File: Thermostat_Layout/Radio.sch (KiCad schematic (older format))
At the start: 15 parts, among them J4 Conn_Coaxial, U6 nRF24L01P, Y2 16MHz

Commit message: Update remote sensor layout
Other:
- moved on the sheet: C10, C11, C12, C13, C14, C8, C9, R8, R9, Y2

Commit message: Remove NRF24 from schematic
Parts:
- removed C10: 2.2nF, Capacitor_SMD:C_0402_1005Metric, symbol Device:C
- removed C11, C9: 22pF, Capacitor_SMD:C_0402_1005Metric, symbol Device:C
- removed C12: 4.7pF, Capacitor_SMD:C_0402_1005Metric, symbol Device:C
- removed C13: 15pF, Capacitor_SMD:C_0402_1005Metric, symbol Device:C
- removed C14: 1.5pF, Capacitor_SMD:C_0402_1005Metric, symbol Device:C
- removed C8: 33nF, Capacitor_SMD:C_0402_1005Metric, symbol Device:C
- removed J4: Conn_Coaxial, Connector_Coaxial:U.FL_Molex_MCRF_73412-0110_Vertical, symbol Connector:Conn_Coaxial
- removed L1: 12nH, Inductor_SMD:L_0402_1005Metric, symbol Device:L
- removed L2: 2.3nH, Inductor_SMD:L_0402_1005Metric, symbol Device:L
- removed L3: 7.9nH, Inductor_SMD:L_0402_1005Metric, symbol Device:L
- removed R8: 22kΩ, Resistors:0402, symbol Device:R_US
- removed R9: 1MΩ, Resistor_SMD:R_0402_1005Metric, symbol Device:R_US
- removed U6: nRF24L01P, Package_DFN_QFN:QFN-20-1EP_4x4mm_P0.5mm_EP2.5x2.5mm, symbol RF:nRF24L01P
- removed Y2: 16MHz, Crystal:Crystal_SMD_SeikoEpson_MC405-2Pin_9.6x4.1mm, symbol Device:Crystal
- added U?: ESP-07, RF_Module:ESP-07, symbol RF_Module:ESP-07
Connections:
- net labels removed: 3.3V, GND, MISO, MOSI, RF_CE, RF_CSN, SCK
- wire segments 42 -> 0

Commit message: Update schematic
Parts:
- gave numbers to parts that had none: 1
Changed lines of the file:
@@
 $EndDescr
 $Comp
-L RF_Module:ESP-07 U?
+L RF_Module:ESP-07 U10
 U 1 1 5D98C19F
 P 5900 3650
-F 0 "U?" H 5900 4631 50  0000 C CNN
+F 0 "U10" H 5900 4631 50  0000 C CNN
 F 1 "ESP-07" H 5900 4540 50  0000 C CNN
 F 2 "RF_Module:ESP-07" H 5900 3650 50  0001 C CNN

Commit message: Layout changes
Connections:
- net RADIO_RST: now reaches U10.1 (~RST)
- net RADIO_RX: now reaches U10.15 (GPIO3/RXD)
- net RADIO_TX: now reaches U10.16 (GPIO1/TXD)
- net RADIO_EN: now reaches U10.3 (EN)
- net 3.3V: now reaches U10.8 (VCC)
- net GND: now reaches U10.9 (GND)
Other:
- moved on the sheet: U10
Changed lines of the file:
@@
 L RF_Module:ESP-07 U10
 U 1 1 5D98C19F
-P 5900 3650
-F 0 "U10" H 5900 4631 50  0000 C CNN
-F 1 "ESP-07" H 5900 4540 50  0000 C CNN
-F 2 "RF_Module:ESP-07" H 5900 3650 50  0001 C CNN
-F 3 "http://wiki.ai-thinker.com/_media/esp8266/esp8266_series_modules_user_manual_v1.1.pdf" H 5550 3750 50  0001 C CNN
-	1    5900 3650
+P 5650 3550
+F 0 "U10" H 5650 4531 50  0000 C CNN
+F 1 "ESP-07" H 5650 4440 50  0000 C CNN
+F 2 "RF_Module:ESP-07" H 5650 3550 50  0001 C CNN
+F 3 "http://wiki.ai-thinker.com/_media/esp8266/esp8266_series_modules_user_manual_v1.1.pdf" H 5300 3650 50  0001 C CNN
+	1    5650 3550
 	1    0    0    -1
 $EndComp
+Text GLabel 6600 3050 2    50   Output ~ 0
+RADIO_TX
+Text GLabel 6600 3250 2    50   Input ~ 0
+RADIO_RX
+Wire Wire Line
+	6250 3050 6600 3050
+Wire Wire Line
+	6250 3250 6600 3250
+$Comp
+L SparkFun-PowerSymbols:3.3V #SUPPLY?
+U 1 1 5D9E7A19
+P 5650 2500
+F 0 "#SUPPLY?" H 5700 2500 45  0001 L BNN
+F 1 "3.3V" H 5650 2776 45  0000 C CNN
+F 2 "XXX-00000" H 5650 2681 60  0000 C CNN
+F 3 "" H 5650 2500 60  0001 C CNN
+	1    5650 2500
+	1    0    0    -1
+$EndComp
+$Comp
+L SparkFun-PowerSymbols:GND #GND?
+U 1 1 5D9E8201
+P 5650 4400
+F 0 "#GND?" H 5700 4350 45  0001 L BNN
+F 1 "GND" H 5650 4230 45  0000 C CNN
+F 2 "" H 5650 4300 60  0001 C CNN
+F 3 "" H 5650 4300 60  0001 C CNN
+	1    5650 4400
+	1    0    0    -1
+$EndComp
+Wire Wire Line
+	5650 4250 5650 4400
+Wire Wire Line
+	5650 2750 5650 2500
+Text GLabel 4650 2950 0    50   Input ~ 0
+RADIO_RST
+Text GLabel 4650 3150 0    50   Input ~ 0
+RADIO_EN
+Wire Wire Line
+	4650 2950 5050 2950
+Wire Wire Line
+	5050 3150 4650 3150
 $EndSCHEMATC

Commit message: Complete radio schematic
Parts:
- added J? (x2): Conn_01x03, symbol Connector_Generic:Conn_01x03
- added R? (x2): 10k, symbol Device:R_US
- added R? (x5): 1k, symbol Device:R_US
- added SW? (x2): SW_DPDT_x2, symbol Switch:SW_DPDT_x2
- added SW? (x2): SW_SPST, symbol Switch:SW_SPST
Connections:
- net 3.3V: now also R?.1, R?.1
- net GND: now also J?.2 (Pin_2), J?.2 (Pin_2), R?.2, SW?.1 (A), SW?.2 (B)
- net RADIO_EN: now also R?.2
- net RADIO_RST: now also R?.2, SW?.2 (B)
- net at U10.10 (GPIO15): now also R?.1
- net at U10.12 (GPIO0): now also SW?.1 (A)
- net DBG_RX: now reaches U10.5 (GPIO14)
- net DBG_RX: now also R?.2
- net DBG_TX: now reaches U10.6 (GPIO12)
- net DBG_TX: now also R?.2
- net RADIO_RX renamed RX
- net RX: now also SW?.5 (B)
- net RADIO_TX renamed TX
- net TX: now also SW?.2 (B)
- new net: J?.1 (Pin_1), R?.1 (x2)
- new net: J?.3 (Pin_3), R?.1 (x2)
- new net RADIO_COM_RX: SW?.4 (A)
- new net RADIO_COM_TX: SW?.1 (A)
- new net RADIO_PRG_RX: R?.2, SW?.6 (C)
- new net RADIO_PRG_TX: R?.2, SW?.3 (C)
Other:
- moved on the sheet: U10

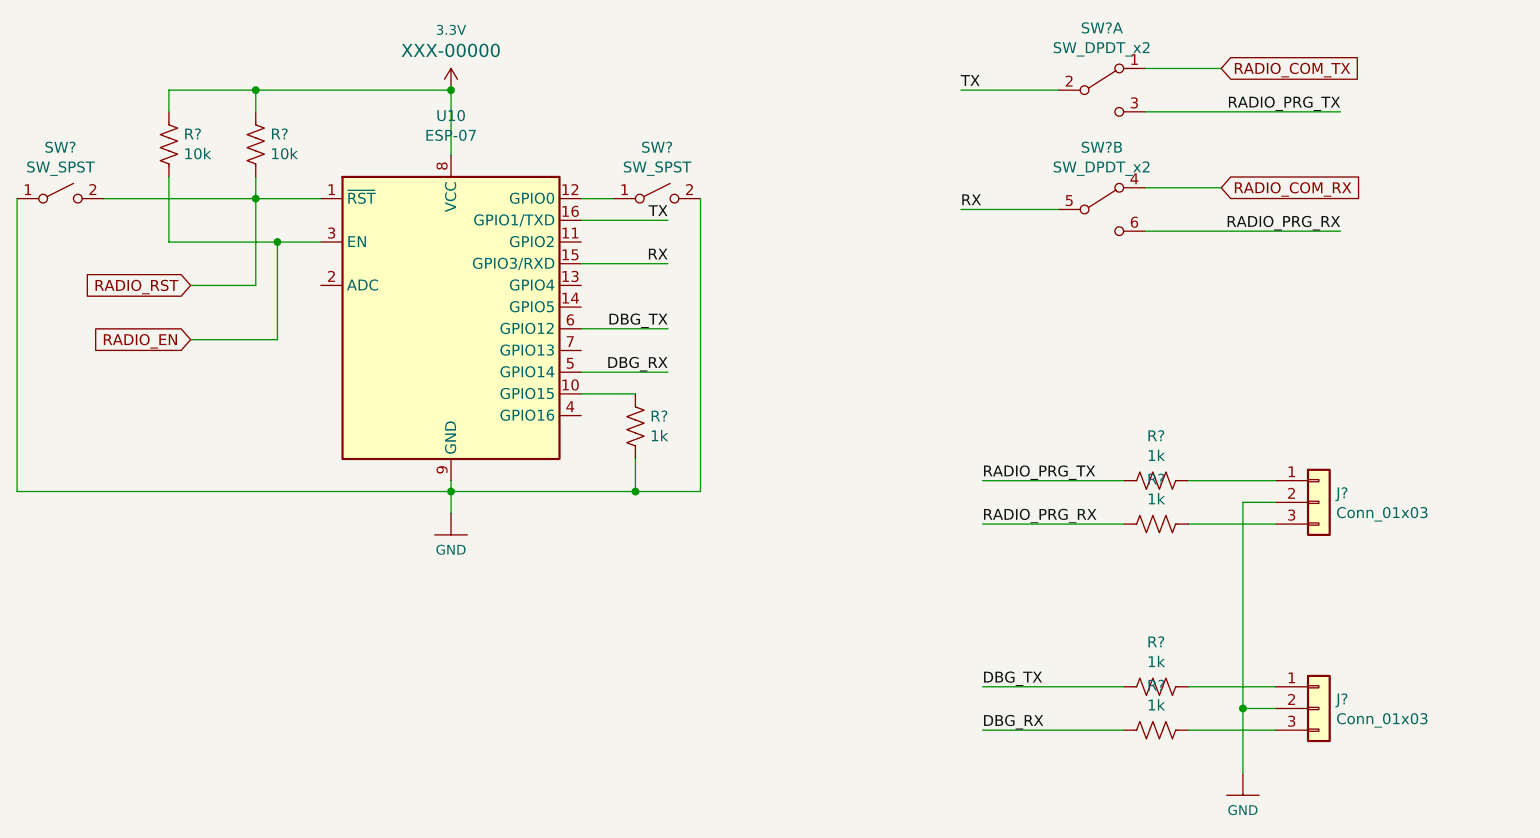
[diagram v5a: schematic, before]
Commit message: FInalize schematic for thermostat
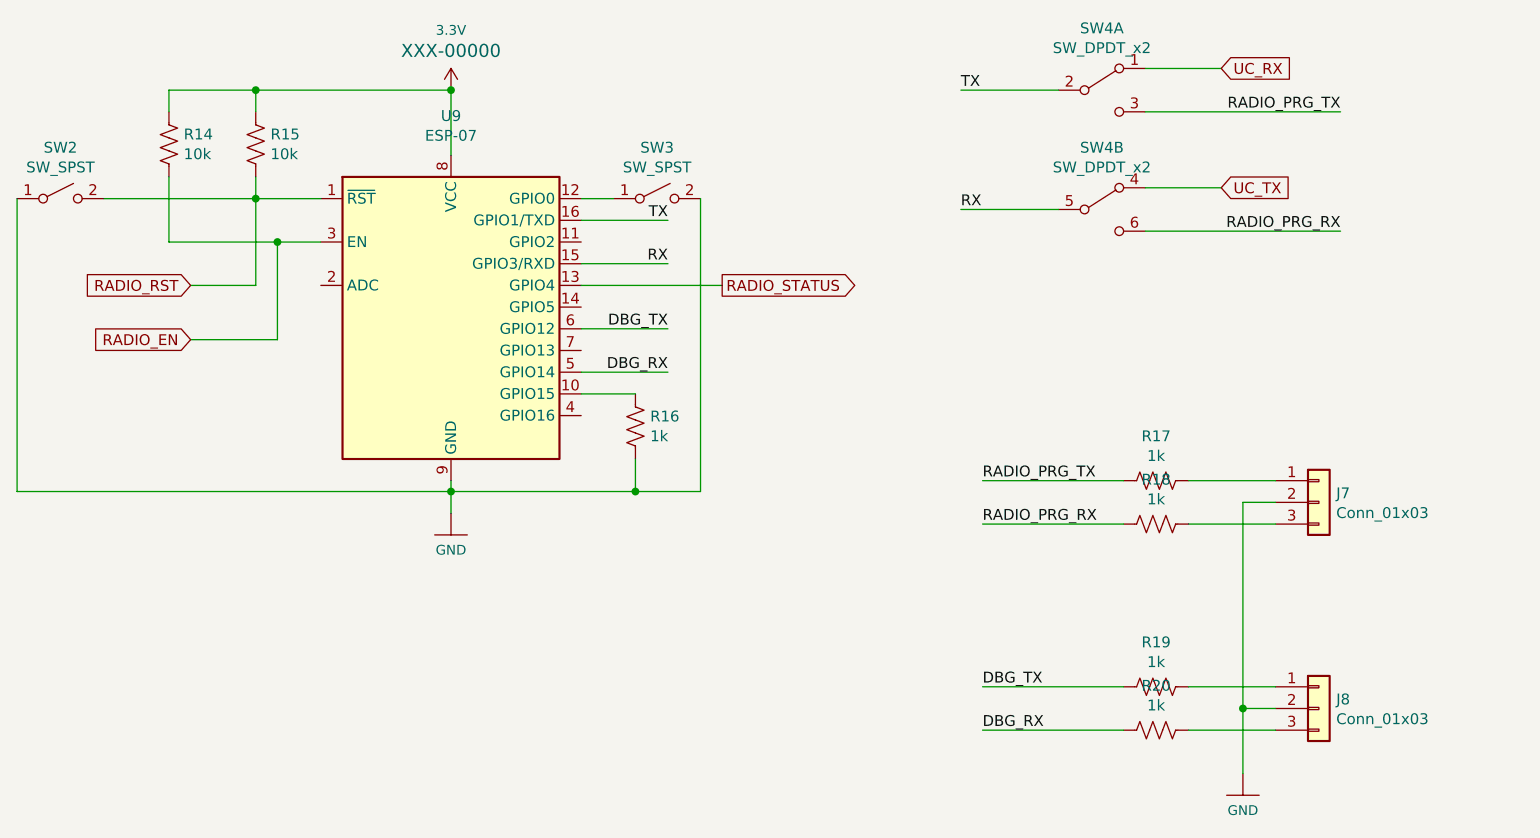
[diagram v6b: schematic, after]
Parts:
- J7, J8: renamed from J?; footprint (none) -> Connector_JST:JST_PH_S3B-PH-SM4-TB_1x03-1MP_P2.00mm_Horizontal
- R14, R15, R16, R17, R18, R19, R20: renamed from R?; footprint (none) -> Resistor_SMD:R_0402_1005Metric
- SW2, SW3: renamed from SW?; footprint (none) -> Button_Switch_SMD:SW_SPST_TL3342
- SW4: renamed from SW?; footprint (none) -> Switches:SWITCH_DPDT_SMD_AYZ0202
- gave numbers to parts that had none: 1
- renumbered U10 to U9
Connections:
- net RADIO_STATUS: now reaches U9.13 (GPIO4)
- net RADIO_COM_RX renamed UC_TX
- net RADIO_COM_TX renamed UC_RX
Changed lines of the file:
@@
 $EndDescr
 $Comp
-L RF_Module:ESP-07 U10
+L RF_Module:ESP-07 U9
 U 1 1 5D98C19F
 P 4400 2850
-F 0 "U10" H 4400 3831 50  0000 C CNN
+F 0 "U9" H 4400 3831 50  0000 C CNN
 F 1 "ESP-07" H 4400 3740 50  0000 C CNN
 F 2 "RF_Module:ESP-07" H 4400 2850 50  0001 C CNN
@@
 $EndComp
 $Comp
-L SparkFun-PowerSymbols:3.3V #SUPPLY?
+L SparkFun-PowerSymbols:3.3V #SUPPLY010
 U 1 1 5D9E7A19
 P 4400 1750
-F 0 "#SUPPLY?" H 4450 1750 45  0001 L BNN
+F 0 "#SUPPLY010" H 4450 1750 45  0001 L BNN
 F 1 "3.3V" H 4400 2026 45  0000 C CNN
 F 2 "XXX-00000" H 4400 1931 60  0000 C CNN
@@
 $EndComp
 $Comp
-L SparkFun-PowerSymbols:GND #GND?
+L SparkFun-PowerSymbols:GND #GND016
 U 1 1 5D9E8201
 P 4400 3700
-F 0 "#GND?" H 4450 3650 45  0001 L BNN
+F 0 "#GND016" H 4450 3650 45  0001 L BNN
 F 1 "GND" H 4400 3530 45  0000 C CNN
 F 2 "" H 4400 3600 60  0001 C CNN
@@
 	4400 3550 4400 3600
 $Comp
-L Switch:SW_DPDT_x2 SW?
+L Switch:SW_DPDT_x2 SW4
 U 1 1 5D9EC108
 P 7400 1750
-F 0 "SW?" H 7400 2035 50  0000 C CNN
+F 0 "SW4" H 7400 2035 50  0000 C CNN
 F 1 "SW_DPDT_x2" H 7400 1944 50  0000 C CNN
 F 2 "" H 7400 1750 50  0001 C CNN
@@
 $EndComp
 $Comp
-L Switch:SW_DPDT_x2 SW?
+L Switch:SW_DPDT_x2 SW4
 U 2 1 5D9ECE92
 P 7400 2300
-F 0 "SW?" H 7400 2585 50  0000 C CNN
+F 0 "SW4" H 7400 2585 50  0000 C CNN
 F 1 "SW_DPDT_x2" H 7400 2494 50  0000 C CNN
-F 2 "" H 7400 2300 50  0001 C CNN
+F 2 "Switches:SWITCH_DPDT_SMD_AYZ0202" H 7400 2300 50  0001 C CNN
 F 3 "~" H 7400 2300 50  0001 C CNN
 	2    7400 2300
@@
 $EndComp
 $Comp
-L Switch:SW_SPST SW?
+L Switch:SW_SPST SW2
 U 1 1 5D9EDB89
 P 2600 2250
-F 0 "SW?" H 2600 2485 50  0000 C CNN
+F 0 "SW2" H 2600 2485 50  0000 C CNN
 F 1 "SW_SPST" H 2600 2394 50  0000 C CNN
-F 2 "" H 2600 2250 50  0001 C CNN
+F 2 "Button_Switch_SMD:SW_SPST_TL3342" H 2600 2250 50  0001 C CNN
 F 3 "~" H 2600 2250 50  0001 C CNN
 	1    2600 2250
@@
 $EndComp
 $Comp
-L Switch:SW_SPST SW?
+L Switch:SW_SPST SW3
 U 1 1 5D9EEB95
 P 5350 2250
-F 0 "SW?" H 5350 2485 50  0000 C CNN
+F 0 "SW3" H 5350 2485 50  0000 C CNN
 F 1 "SW_SPST" H 5350 2394 50  0000 C CNN
-F 2 "" H 5350 2250 50  0001 C CNN
+F 2 "Button_Switch_SMD:SW_SPST_TL3342" H 5350 2250 50  0001 C CNN
 F 3 "~" H 5350 2250 50  0001 C CNN
 	1    5350 2250
@@
 	5400 2550 5000 2550
 $Comp
-L Device:R_US R?
+L Device:R_US R15
 U 1 1 5D9F314E
 P 3500 2000
-F 0 "R?" H 3568 2046 50  0000 L CNN
+F 0 "R15" H 3568 2046 50  0000 L CNN
 F 1 "10k" H 3568 1955 50  0000 L CNN
-F 2 "" V 3540 1990 50  0001 C CNN
+F 2 "Resistor_SMD:R_0402_1005Metric" V 3540 1990 50  0001 C CNN
 F 3 "~" H 3500 2000 50  0001 C CNN
 	1    3500 2000
@@
 $EndComp
 $Comp
-L Device:R_US R?
+L Device:R_US R14
 U 1 1 5D9F3994
 P 3100 2000
-F 0 "R?" H 3168 2046 50  0000 L CNN
+F 0 "R14" H 3168 2046 50  0000 L CNN
 F 1 "10k" H 3168 1955 50  0000 L CNN
-F 2 "" V 3140 1990 50  0001 C CNN
+F 2 "Resistor_SMD:R_0402_1005Metric" V 3140 1990 50  0001 C CNN
 F 3 "~" H 3100 2000 50  0001 C CNN
 	1    3100 2000
@@
 	7600 2200 7950 2200
 $Comp
-L Device:R_US R?
+L Device:R_US R16
 U 1 1 5D9FB4B8
 P 5250 3300
-F 0 "R?" H 5318 3346 50  0000 L CNN
+F 0 "R16" H 5318 3346 50  0000 L CNN
 F 1 "1k" H 5318 3255 50  0000 L CNN
-F 2 "" V 5290 3290 50  0001 C CNN
+F 2 "Resistor_SMD:R_0402_1005Metric" V 5290 3290 50  0001 C CNN
 F 3 "~" H 5250 3300 50  0001 C CNN
 	1    5250 3300
@@
 	5250 3600 4400 3600
 Text GLabel 7950 1650 2    50   Input ~ 0
-RADIO_COM_TX
+UC_RX
 Text GLabel 7950 2200 2    50   Input ~ 0
-RADIO_COM_RX
+UC_TX
 Text Label 8500 1850 2    50   ~ 0
 RADIO_PRG_TX
@@
 RADIO_PRG_RX
 $Comp
-L Connector_Generic:Conn_01x03 J?
+L Connector_Generic:Conn_01x03 J7
 U 1 1 5DA11398
 P 8400 3650
-F 0 "J?" H 8480 3692 50  0000 L CNN
+F 0 "J7" H 8480 3692 50  0000 L CNN
 F 1 "Conn_01x03" H 8480 3601 50  0000 L CNN
-F 2 "" H 8400 3650 50  0001 C CNN
+F 2 "Connector_JST:JST_PH_S3B-PH-SM4-TB_1x03-1MP_P2.00mm_Horizontal" H 8400 3650 50  0001 C CNN
 F 3 "~" H 8400 3650 50  0001 C CNN
 	1    8400 3650
@@
 $EndComp
 $Comp
-L Device:R_US R?
+L Device:R_US R17
 U 1 1 5DA1198B
 P 7650 3550
-F 0 "R?" V 7445 3550 50  0000 C CNN
+F 0 "R17" V 7445 3550 50  0000 C CNN
 F 1 "1k" V 7536 3550 50  0000 C CNN
-F 2 "" V 7690 3540 50  0001 C CNN
+F 2 "Resistor_SMD:R_0402_1005Metric" V 7690 3540 50  0001 C CNN
 F 3 "~" H 7650 3550 50  0001 C CNN
 	1    7650 3550
@@
 $EndComp
 $Comp
-L Device:R_US R?
+L Device:R_US R18
 U 1 1 5DA12147
 P 7650 3750
-F 0 "R?" V 7445 3750 50  0000 C CNN
+F 0 "R18" V 7445 3750 50  0000 C CNN
 F 1 "1k" V 7536 3750 50  0000 C CNN
-F 2 "" V 7690 3740 50  0001 C CNN
+F 2 "Resistor_SMD:R_0402_1005Metric" V 7690 3740 50  0001 C CNN
 F 3 "~" H 7650 3750 50  0001 C CNN
 	1    7650 3750
@@
 	5000 2850 5400 2850
 $Comp
-L Connector_Generic:Conn_01x03 J?
+L Connector_Generic:Conn_01x03 J8
 U 1 1 5DA1AC6B
 P 8400 4600
-F 0 "J?" H 8480 4642 50  0000 L CNN
+F 0 "J8" H 8480 4642 50  0000 L CNN
 F 1 "Conn_01x03" H 8480 4551 50  0000 L CNN
-F 2 "" H 8400 4600 50  0001 C CNN
+F 2 "Connector_JST:JST_PH_S3B-PH-SM4-TB_1x03-1MP_P2.00mm_Horizontal" H 8400 4600 50  0001 C CNN
 F 3 "~" H 8400 4600 50  0001 C CNN
 	1    8400 4600
@@
 $EndComp
 $Comp
-L Device:R_US R?
+L Device:R_US R20
 U 1 1 5DA1E49D
 P 7650 4700
-F 0 "R?" V 7445 4700 50  0000 C CNN
+F 0 "R20" V 7445 4700 50  0000 C CNN
 F 1 "1k" V 7536 4700 50  0000 C CNN
-F 2 "" V 7690 4690 50  0001 C CNN
+F 2 "Resistor_SMD:R_0402_1005Metric" V 7690 4690 50  0001 C CNN
 F 3 "~" H 7650 4700 50  0001 C CNN
 	1    7650 4700
@@
 $EndComp
 $Comp
-L Device:R_US R?
+L Device:R_US R19
 U 1 1 5DA1C18D
 P 7650 4500
-F 0 "R?" V 7445 4500 50  0000 C CNN
+F 0 "R19" V 7445 4500 50  0000 C CNN
 F 1 "1k" V 7536 4500 50  0000 C CNN
-F 2 "" V 7690 4490 50  0001 C CNN
+F 2 "Resistor_SMD:R_0402_1005Metric" V 7690 4490 50  0001 C CNN
 F 3 "~" H 7650 4500 50  0001 C CNN
 	1    7650 4500
@@
 Connection ~ 8050 4600
 $Comp
-L SparkFun-PowerSymbols:GND #GND?
+L SparkFun-PowerSymbols:GND #GND017
 U 1 1 5DA21A27
 P 8050 4900
-F 0 "#GND?" H 8100 4850 45  0001 L BNN
+F 0 "#GND017" H 8100 4850 45  0001 L BNN
 F 1 "GND" H 8050 4730 45  0000 C CNN
 F 2 "" H 8050 4800 60  0001 C CNN
@@
 Text Label 6850 4700 0    50   ~ 0
 DBG_RX
+Text GLabel 5650 2650 2    50   Output ~ 0
+RADIO_STATUS
+Wire Wire Line
+	5000 2650 5650 2650
 $EndSCHEMATC

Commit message: Schematic and PCB layout for thermostat
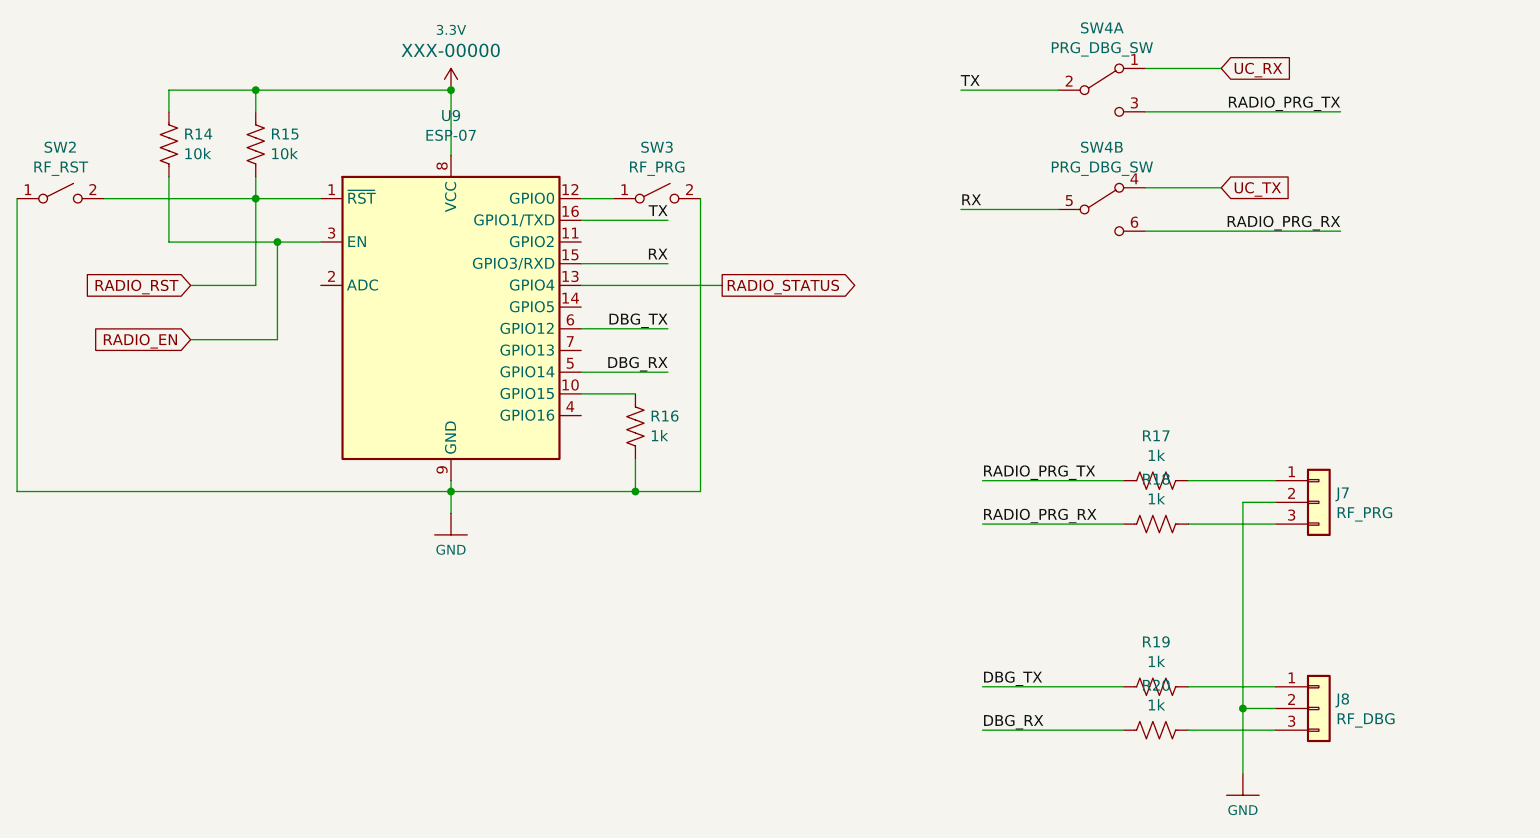
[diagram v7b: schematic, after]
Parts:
- J7: value Conn_01x03 -> RF_PRG; footprint Connector_JST:JST_PH_S3B-PH-SM4-TB_1x03-1MP_P2.00mm_Horizontal -> Connector_JST:JST_EH_B3B-EH-A_1x03_P2.50mm_Vertical
- J8: value Conn_01x03 -> RF_DBG; footprint Connector_JST:JST_PH_S3B-PH-SM4-TB_1x03-1MP_P2.00mm_Horizontal -> Connector_JST:JST_EH_B3B-EH-A_1x03_P2.50mm_Vertical
- SW2: value SW_SPST -> RF_RST
- SW3: value SW_SPST -> RF_PRG
- SW4: value SW_DPDT_x2 -> PRG_DBG_SW
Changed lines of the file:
@@
 P 7400 1750
 F 0 "SW4" H 7400 2035 50  0000 C CNN
-F 1 "SW_DPDT_x2" H 7400 1944 50  0000 C CNN
+F 1 "PRG_DBG_SW" H 7400 1944 50  0000 C CNN
 F 2 "" H 7400 1750 50  0001 C CNN
 F 3 "~" H 7400 1750 50  0001 C CNN
@@
 P 7400 2300
 F 0 "SW4" H 7400 2585 50  0000 C CNN
-F 1 "SW_DPDT_x2" H 7400 2494 50  0000 C CNN
+F 1 "PRG_DBG_SW" H 7400 2494 50  0000 C CNN
 F 2 "Switches:SWITCH_DPDT_SMD_AYZ0202" H 7400 2300 50  0001 C CNN
 F 3 "~" H 7400 2300 50  0001 C CNN
@@
 P 2600 2250
 F 0 "SW2" H 2600 2485 50  0000 C CNN
-F 1 "SW_SPST" H 2600 2394 50  0000 C CNN
+F 1 "RF_RST" H 2600 2394 50  0000 C CNN
 F 2 "Button_Switch_SMD:SW_SPST_TL3342" H 2600 2250 50  0001 C CNN
 F 3 "~" H 2600 2250 50  0001 C CNN
@@
 P 5350 2250
 F 0 "SW3" H 5350 2485 50  0000 C CNN
-F 1 "SW_SPST" H 5350 2394 50  0000 C CNN
+F 1 "RF_PRG" H 5350 2394 50  0000 C CNN
 F 2 "Button_Switch_SMD:SW_SPST_TL3342" H 5350 2250 50  0001 C CNN
 F 3 "~" H 5350 2250 50  0001 C CNN
@@
 P 8400 3650
 F 0 "J7" H 8480 3692 50  0000 L CNN
-F 1 "Conn_01x03" H 8480 3601 50  0000 L CNN
-F 2 "Connector_JST:JST_PH_S3B-PH-SM4-TB_1x03-1MP_P2.00mm_Horizontal" H 8400 3650 50  0001 C CNN
+F 1 "RF_PRG" H 8480 3601 50  0000 L CNN
+F 2 "Connector_JST:JST_EH_B3B-EH-A_1x03_P2.50mm_Vertical" H 8400 3650 50  0001 C CNN
 F 3 "~" H 8400 3650 50  0001 C CNN
 	1    8400 3650
@@
 P 8400 4600
 F 0 "J8" H 8480 4642 50  0000 L CNN
-F 1 "Conn_01x03" H 8480 4551 50  0000 L CNN
-F 2 "Connector_JST:JST_PH_S3B-PH-SM4-TB_1x03-1MP_P2.00mm_Horizontal" H 8400 4600 50  0001 C CNN
+F 1 "RF_DBG" H 8480 4551 50  0000 L CNN
+F 2 "Connector_JST:JST_EH_B3B-EH-A_1x03_P2.50mm_Vertical" H 8400 4600 50  0001 C CNN
 F 3 "~" H 8400 4600 50  0001 C CNN
 	1    8400 4600
